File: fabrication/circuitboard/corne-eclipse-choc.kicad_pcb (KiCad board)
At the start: 2 copper layers, 275.5 x 105.6 mm, 182 parts, among them J2 OLED, J4 OLED, SW1 SW_Choc_v1v2_HS, SW10 SW_Choc_v1v2_HS, SW11 SW_Choc_v1v2_HS, SW12 SW_Choc_v1v2_HS, SW13 SW_Choc_v1v2_HS, SW14 SW_Choc_v1v2_HS, SW15 SW_Choc_v1v2_HS, SW16 SW_Choc_v1v2_HS, SW17 SW_Choc_v1v2_HS, SW18 SW_Choc_v1v2_HS, SW2 SW_Choc_v1v2_HS, SW20 SW_Choc_v1v2_HS, SW21 SW_Choc_v1v2_HS, SW22 SW_Choc_v1v2_HS, SW23 SW_Choc_v1v2_HS, SW24 SW_Choc_v1v2_HS, SW25 SW_Choc_v1v2_HS, SW26 SW_Choc_v1v2_HS, SW27 SW_Choc_v1v2_HS, SW28 SW_Choc_v1v2_HS, SW29 SW_Choc_v1v2_HS, SW3 SW_Choc_v1v2_HS, SW30 SW_Choc_v1v2_HS, SW31 SW_Choc_v1v2_HS, SW32 SW_Choc_v1v2_HS, SW33 SW_Choc_v1v2_HS, SW34 SW_Choc_v1v2_HS, SW35 SW_Choc_v1v2_HS, SW36 SW_Choc_v1v2_HS, SW37 SW_Choc_v1v2_HS, SW38 SW_Choc_v1v2_HS, SW39 SW_Choc_v1v2_HS, SW4 SW_Choc_v1v2_HS, SW40 SW_Choc_v1v2_HS, SW42 SW_Choc_v1v2_HS, SW43 SW_Choc_v1v2_HS, SW44 SW_Choc_v1v2_HS, SW5 SW_Choc_v1v2_HS, SW6 SW_Choc_v1v2_HS, SW7 SW_Choc_v1v2_HS, SW8 SW_Choc_v1v2_HS, SW9 SW_Choc_v1v2_HS, U1 nice!nano, U2 nice!nano

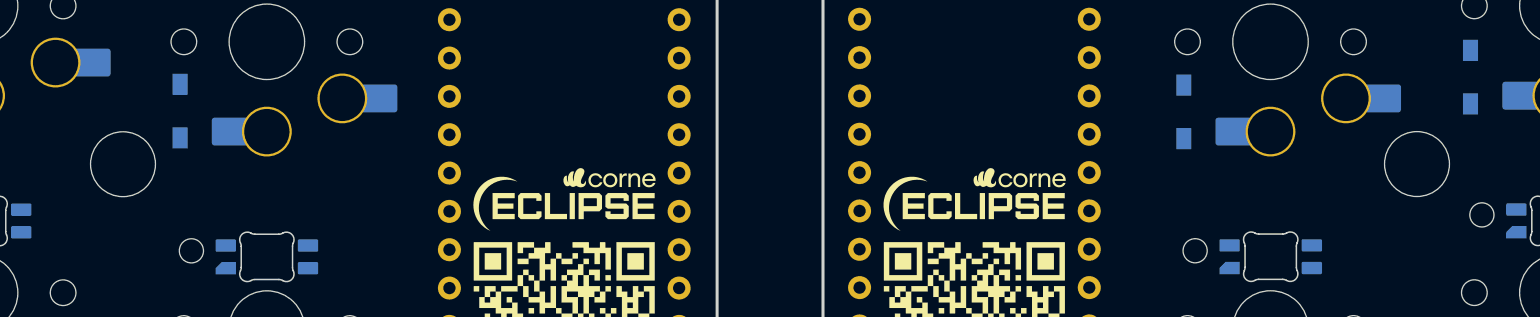
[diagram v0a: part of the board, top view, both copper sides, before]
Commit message: fix(pcb): screw hole alignment to case adjustments
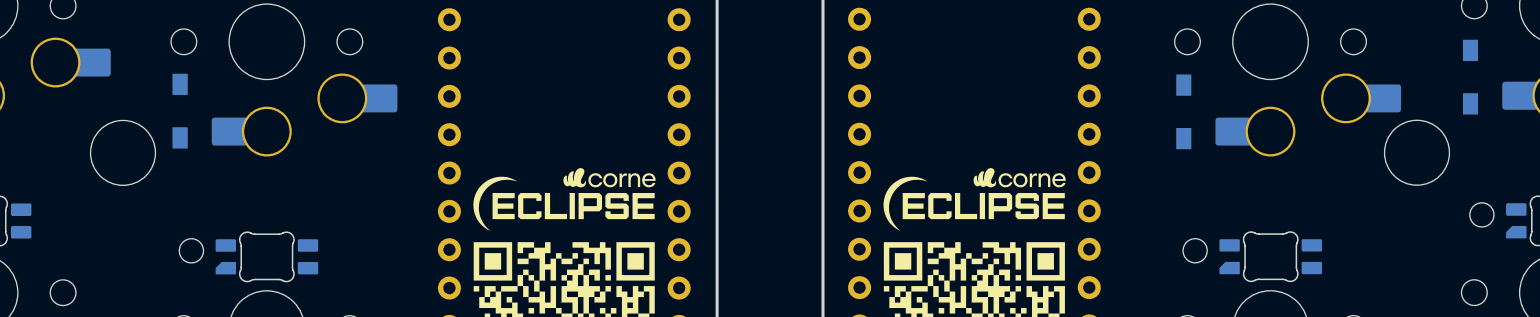
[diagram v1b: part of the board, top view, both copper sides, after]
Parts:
- moved MH1 0.75 mm to (105.6, 40.0)
- moved MH9 0.75 mm to (191.3, 40.0)

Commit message: wip: rgb/choc
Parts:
- moved GLOW06 23.2 mm to (118.5, 97.2)
- moved GLOW02 22.7 mm to (29.8, 32.1)
- moved GLOW01 19.3 mm to (51.0, 38.2)
- moved GLOW03 14.8 mm to (20.2, 63.4), turned to 0 degrees
- moved GLOW05 5.63 mm to (67.2, 77.7), turned to 0 degrees
- moved GLOW04 1.01 mm to (46.3, 64.4), turned to 0 degrees

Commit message: fix(pcbs): aligned screw holes on lp and mx
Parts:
- added BT1: Breakaway_Tabs, kbd:Breakaway_Tabs, F.Cu at (187.0, 20.9)
- added BT2: Breakaway_Tabs, kbd:Breakaway_Tabs, F.Cu at (225.0, 20.9)
- added BT3: Breakaway_Tabs, kbd:Breakaway_Tabs, F.Cu at (148.9, 82.2)
- added BT4: Breakaway_Tabs, kbd:Breakaway_Tabs, F.Cu at (170.9, 82.2)
- added ENC1: ENC_SW_EC12_Choc, Corne Eclipse:ENC_SW_EC12_Choc_v1v2_HS_1u, F.Cu at (196.0, 87.6)
- added J2: OLED, corne:nice!view, F.Cu at (258.3, 62.7)
- added MH1: Val**, kbd:M2_HOLE_v2, F.Cu at (234.3, 40.2)
- added MH10: Val**, kbd:M2_HOLE_v2, F.Cu at (156.3, 53.4)
- added MH11: Val**, kbd:M2_HOLE_v2, F.Cu at (158.4, 44.5)
- added MH12: Val**, kbd:M2_HOLE_v2, B.Cu at (283.3, 82.2)
- added MH2: Val**, kbd:M2_HOLE_v2, F.Cu at (201.5, 80.6)
- added MH3: Val**, kbd:M2_HOLE_v2, F.Cu at (248.1, 88.4)
- added MH4: Val**, kbd:M2_HOLE_v2, F.Cu at (256.6, 73.3)
- added MH5: Val**, kbd:M2_HOLE_v2, F.Cu at (271.0, 81.8)
- added PWR1: , corne:power, F.Cu at (271.8, 74.9)
- added RSW1: SW_PUSH, kbd:ResetSW_1side, F.Cu at (271.5, 65.2)
- added RSW2: SW_PUSH, kbd:ResetSW_1side, F.Cu at (282.9, 65.6)
- added SW1: SW_Choc_v1v2_HS, Corne Eclipse:SW_Choc_v1v2_HS_1u, F.Cu at (148.9, 34.8)
- added SW10: SW_Choc_v1v2_HS, Corne Eclipse:SW_Choc_v1v2_HS_1u, F.Cu at (205.9, 46.7)
- added SW11: SW_Choc_v1v2_HS, Corne Eclipse:SW_Choc_v1v2_HS_1u, F.Cu at (224.9, 49.1)
- added SW12: SW_Choc_v1v2_HS, Corne Eclipse:SW_Choc_v1v2_HS_1u, F.Cu at (243.9, 51.5)
- added SW13: SW_Choc_v1v2_HS, Corne Eclipse:SW_Choc_v1v2_HS_1u, F.Cu at (148.9, 72.8)
- added SW14: SW_Choc_v1v2_HS, Corne Eclipse:SW_Choc_v1v2_HS_1u, F.Cu at (167.9, 72.8)
- added SW15: SW_Choc_v1v2_HS, Corne Eclipse:SW_Choc_v1v2_HS_1u, F.Cu at (186.9, 68.1)
- added SW16: SW_Choc_v1v2_HS, Corne Eclipse:SW_Choc_v1v2_HS_1u, F.Cu at (203.2, 75.1)
- added SW17: SW_Choc_v1v2_HS, Corne Eclipse:SW_Choc_v1v2_HS_1u, F.Cu at (224.9, 68.1)
- added SW18: SW_Choc_v1v2_HS, Corne Eclipse:SW_Choc_v1v2_HS_1u, F.Cu at (243.9, 70.5)
- added SW2: SW_Choc_v1v2_HS, Corne Eclipse:SW_Choc_v1v2_HS_1u, F.Cu at (167.9, 34.8)
- added SW20: SW_Choc_v1v2_HS, Corne Eclipse:SW_Choc_v1v2_HS_1u, F.Cu at (215.4, 87.7)
- added SW21: SW_Choc_v1v2_HS, Corne Eclipse:SW_Choc_v1v2_HS_1u, F.Cu at (236.4, 90.5)
- added SW22: SW_Choc_v1v2_HS, Corne Eclipse:SW_Choc_v1v2_HS_1.5u, F.Cu at (258.6, 94.2)
- added SW3: SW_Choc_v1v2_HS, Corne Eclipse:SW_Choc_v1v2_HS_1u, F.Cu at (186.9, 30.1)
- added SW4: SW_Choc_v1v2_HS, Corne Eclipse:SW_Choc_v1v2_HS_1u, F.Cu at (205.9, 27.7)
- added SW5: SW_Choc_v1v2_HS, Corne Eclipse:SW_Choc_v1v2_HS_1u, F.Cu at (224.9, 30.1)
- added SW6: SW_Choc_v1v2_HS, Corne Eclipse:SW_Choc_v1v2_HS_1u, F.Cu at (243.9, 32.5)
- added SW7: SW_Choc_v1v2_HS, Corne Eclipse:SW_Choc_v1v2_HS_1u, F.Cu at (148.9, 53.8)
- added SW8: SW_Choc_v1v2_HS, Corne Eclipse:SW_Choc_v1v2_HS_1u, F.Cu at (167.9, 53.8)
- added SW9: SW_Choc_v1v2_HS, Corne Eclipse:SW_Choc_v1v2_HS_1u, F.Cu at (186.9, 49.1)
- added TP2: Tenting Puck, Corne Eclipse:Tenting_Puck, F.Cu at (216.2, 57.6)
- added U1: nice!nano, kbd:ProMicro_v3, F.Cu at (263.6, 45.5)
- moved GLOW06 23.2 mm to (103.7, 79.3)
- moved GLOW02 22.7 mm to (51.3, 39.5)
- moved GLOW01 19.3 mm to (70.2, 36.5)
- moved GLOW03 14.8 mm to (29.2, 51.7), turned to 90 degrees
- moved SW16 9.81 mm to (74.4, 75.1)
- moved GLOW05 5.63 mm to (72.8, 78.2), turned to 90 degrees
- moved GLOW04 1.01 mm to (46.8, 63.5), turned to 90 degrees
- moved MH13 0.57 mm to (269.4, 53.7)
- moved MH8 0.57 mm to (267.3, 44.9)
- moved MH9 0.52 mm to (191.3, 40.5)
- moved BT5 0.37 mm to (276.7, 82.6)
- moved MH12 0.37 mm to (154.6, 82.2)
- moved MH14 0.37 mm to (169.0, 73.6)
- moved MH6 0.37 mm to (177.6, 88.8)
- moved SW35 0.37 mm to (276.6, 73.2)
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
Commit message: wip(pcbs): choc layout done, mx layout started
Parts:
- removed the BT1 at (187.0, 20.9)
- removed the BT2 at (225.0, 20.9)
- removed the BT3 at (148.9, 82.2)
- removed the BT4 at (170.9, 82.2)
- removed the ENC1 at (196.0, 87.6)
- removed the J2 at (258.3, 62.7)
- removed the MH1 at (234.3, 40.2)
- removed the MH10 at (156.3, 53.4)
- removed the MH11 at (158.4, 44.5)
- removed the MH12 at (283.3, 82.2)
- removed the MH2 at (201.5, 80.6)
- removed the MH3 at (248.1, 88.4)
- removed the MH4 at (256.6, 73.3)
- removed the MH5 at (271.0, 81.8)
- removed the PWR1 at (271.8, 74.9)
- removed the RSW1 at (271.5, 65.2)
- removed the RSW2 at (282.9, 65.6)
- removed the SW1 at (148.9, 34.8)
- removed the SW10 at (205.9, 46.7)
- removed the SW11 at (224.9, 49.1)
- removed the SW12 at (243.9, 51.5)
- removed the SW13 at (148.9, 72.8)
- removed the SW14 at (167.9, 72.8)
- removed the SW15 at (186.9, 68.1)
- removed the SW16 at (203.2, 75.1)
- removed the SW17 at (224.9, 68.1)
- removed the SW18 at (243.9, 70.5)
- removed the SW2 at (167.9, 34.8)
- removed the SW20 at (215.4, 87.7)
- removed the SW21 at (236.4, 90.5)
- removed the SW22 at (258.6, 94.2)
- removed the SW3 at (186.9, 30.1)
- removed the SW4 at (205.9, 27.7)
- removed the SW5 at (224.9, 30.1)
- removed the SW6 at (243.9, 32.5)
- removed the SW7 at (148.9, 53.8)
- removed the SW8 at (167.9, 53.8)
- removed the SW9 at (186.9, 49.1)
- removed the TP2 at (216.2, 57.6)
- removed the U1 at (263.6, 45.5)
- moved GLOW01 22.4 mm to (118.0, 96.6)
- moved GLOW01 22.4 mm to (178.7, 96.6), turned to -90 degrees
- moved GLOW06 20.0 mm to (86.8, 25.3)
- moved GLOW06 19.9 mm to (210.0, 25.3), turned to -90 degrees
- moved GLOW04 19.5 mm to (29.5, 32.2)
- moved GLOW04 19.5 mm to (267.2, 32.2), turned to -90 degrees
- moved SW16 9.46 mm to (77.1, 66.0)
- moved GLOW02 7.70 mm to (231.7, 77.9), turned to 0 degrees
- moved GLOW02 7.69 mm to (65.1, 77.9), turned to 0 degrees
- moved D19B 7.24 mm to (56.9, 87.5)
- moved D4 4.24 mm to (71.6, 32.0)
- moved D3 1.50 mm to (50.4, 31.8)
- moved GLOW03 0.67 mm to (47.4, 63.6), turned to 0 degrees
- moved GLOW03 0.66 mm to (249.3, 63.6), turned to 0 degrees
- moved D5 0.51 mm to (90.6, 34.3)
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- renumbered GLOW06 to GLOW01, GLOW05 to GLOW02, GLOW04 to GLOW03, GLOW03 to GLOW04, GLOW02 to GLOW05, GLOW01 to GLOW06, SHINE04 to SHINE01, SHINE05 to SHINE02, SHINE12 to SHINE03, SHINE13 to SHINE04, SHINE18 to SHINE05, SHINE19 to SHINE06, SHINE20 to SHINE07, SHINE17 to SHINE08, SHINE14 to SHINE09, SHINE11 to SHINE10, SHINE06 to SHINE11, SHINE03 to SHINE12, SHINE02 to SHINE13, SHINE07 to SHINE14, SHINE10 to SHINE15, SHINE15 to SHINE16, SHINE16 to SHINE17, SHINE21 to SHINE18, SHINE09 to SHINE19, SHINE08 to SHINE20, SHINE01 to SHINE21
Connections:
- GLOW01 pad next: led6-led7 -> led23-led24
- GLOW01 pad prev: led5-led6 -> led21-led23
- GLOW01 pad next: led34-led35 -> led51-led52
- GLOW01 pad prev: led33-led34 -> led49-led51
- GLOW02 pad next: led5-led6 -> led24-led25
- GLOW02 pad prev: led4-led5 -> led23-led24
- GLOW02 pad next: led33-led34 -> led52-led53
- GLOW02 pad prev: led32-led33 -> led51-led52
- GLOW03 pad next: led32-led33 -> led53-led54
- GLOW03 pad prev: led31-led32 -> led52-led53
- GLOW03 pad next: led4-led5 -> led25-led26
- GLOW03 pad prev: led3-led4 -> led24-led25
- GLOW04 pad next: led3-led4 -> led26-led27
- GLOW04 pad prev: led2-led3 -> led25-led26
- GLOW04 pad next: led31-led32 -> led54-led55
- GLOW04 pad prev: led30-led31 -> led53-led54
- GLOW05 pad next: led2-led3 -> led27-led28
- GLOW05 pad prev: led1-led2 -> led26-led27
- GLOW05 pad next: led30-led31 -> led55-led56
- GLOW05 pad prev: led29-led30 -> led54-led55
- GLOW06 pad next: led1-led2 -> (no net)
- GLOW06 pad prev: LED -> led27-led28
- GLOW06 pad next: led29-led30 -> (no net)
- GLOW06 pad prev: LED_r -> led55-led56
- SHINE01 pad 1: led9-led10 -> LED
- SHINE01 pad 4: led10-led11 -> led1-led2
- SHINE01 pad 1: led37-led38 -> LED_r
- SHINE01 pad 4: led38-led39 -> led29-led30
- SHINE02 pad 1: led10-led11 -> led1-led2
- SHINE02 pad 4: led11-led12 -> led2-led3
- SHINE02 pad 1: led38-led39 -> led29-led30
- SHINE02 pad 4: led39-led40 -> led30-led31
- SHINE03 pad 1: led17-led18 -> led2-led3
- SHINE03 pad 4: led18-led19 -> led3-led4
- SHINE03 pad 1: led45-led46 -> led30-led31
- SHINE03 pad 4: led46-led47 -> led31-led32
- SHINE04 pad 1: led18-led19 -> led3-led4
- SHINE04 pad 4: led19-led20 -> led4-led5
- SHINE04 pad 1: led46-led47 -> led31-led32
- SHINE04 pad 4: led47-led48 -> led32-led33
- SHINE05 pad 1: led24-led25 -> led4-led5
- SHINE05 pad 4: led25-led26 -> led5-led6
- SHINE05 pad 1: led52-led53 -> led32-led33
- SHINE05 pad 4: led53-led54 -> led33-led34
- SHINE06 pad 1: led25-led26 -> led5-led6
- SHINE06 pad 4: led26-led27 -> led6-led7
- SHINE06 pad 1: led53-led54 -> led33-led34
- SHINE06 pad 4: led54-led55 -> led34-led35
- SHINE07 pad 1: led26-led27 -> led6-led7
- SHINE07 pad 4: led27-led28 -> led7-led8
- SHINE07 pad 1: led54-led55 -> led34-led35
- SHINE07 pad 4: led55-led56 -> led35-led36
- SHINE08 pad 1: led23-led24 -> led7-led8
- SHINE08 pad 4: led24-led25 -> led8-led9
- SHINE08 pad 1: led51-led52 -> led35-led36
- SHINE08 pad 4: led52-led53 -> led36-led37
- SHINE09 pad 1: led19-led20 -> led8-led9
- SHINE09 pad 4: led20-led21 -> led9-led10
- SHINE09 pad 1: led47-led48 -> led36-led37
- SHINE09 pad 4: led48-led49 -> led37-led38
- SHINE10 pad 1: led16-led17 -> led9-led10
- SHINE10 pad 4: led17-led18 -> led10-led11
- SHINE10 pad 1: led44-led45 -> led37-led38
- SHINE10 pad 4: led45-led46 -> led38-led39
- SHINE11 pad 1: led11-led12 -> led10-led11
- SHINE11 pad 4: led12-led13 -> led11-led12
- SHINE11 pad 1: led39-led40 -> led38-led39
- SHINE11 pad 4: led40-led41 -> led39-led40
- SHINE12 pad 1: led8-led9 -> led11-led12
- SHINE12 pad 4: led9-led10 -> led12-led13
- SHINE12 pad 1: led36-led37 -> led39-led40
- SHINE12 pad 4: led37-led38 -> led40-led41
- SHINE13 pad 1: led7-led8 -> led12-led13
- SHINE13 pad 4: led8-led9 -> led13-led14
- SHINE13 pad 1: led35-led36 -> led40-led41
- SHINE13 pad 4: led36-led37 -> led41-led42
- SHINE14 pad 1: led40-led41 -> led41-led42
- SHINE14 pad 4: led41-led42 -> led42-led43
- SHINE14 pad 1: led12-led13 -> led13-led14
- SHINE14 pad 4: led13-led14 -> led14-led15
- SHINE15 pad 1: led15-led16 -> led14-led15
- SHINE15 pad 4: led16-led17 -> led15-led16
- SHINE15 pad 1: led43-led44 -> led42-led43
- SHINE15 pad 4: led44-led45 -> led43-led44
- SHINE16 pad 1: led20-led21 -> led15-led16
- SHINE16 pad 4: led21-led23 -> led16-led17
- SHINE16 pad 1: led48-led49 -> led43-led44
- SHINE16 pad 4: led49-led51 -> led44-led45
- SHINE17 pad 1: led21-led23 -> led16-led17
- SHINE17 pad 4: led23-led24 -> led17-led18
- SHINE17 pad 1: led49-led51 -> led44-led45
- SHINE17 pad 4: led51-led52 -> led45-led46
- SHINE18 pad 1: led27-led28 -> led17-led18
- SHINE18 pad 4: (no net) -> led18-led19
- SHINE18 pad 1: led55-led56 -> led45-led46
- SHINE18 pad 4: (no net) -> led46-led47
- SHINE19 pad 1: led42-led43 -> led46-led47
- SHINE19 pad 4: led43-led44 -> led47-led48
- SHINE19 pad 1: led14-led15 -> led18-led19
- SHINE19 pad 4: led15-led16 -> led19-led20
- SHINE20 pad 1: led41-led42 -> led47-led48
- SHINE20 pad 4: led42-led43 -> led48-led49
- SHINE20 pad 1: led13-led14 -> led19-led20
- SHINE20 pad 4: led14-led15 -> led20-led21
- SHINE21 pad 1: led6-led7 -> led20-led21
- SHINE21 pad 4: led7-led8 -> led21-led23
- SHINE21 pad 1: led34-led35 -> led48-led49
- SHINE21 pad 4: led35-led36 -> led49-led51

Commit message: feat(pcb): wiring ready
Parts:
- moved R2 1.01 mm to (170.1, 69.0)
- moved RGBMOS 1.01 mm to (170.1, 65.8)
- moved R1 1.00 mm to (126.7, 69.0)
- moved RGBMOS 1.00 mm to (126.7, 65.8)
- moved J4 0.56 mm to (156.7, 62.6)
- moved GLOW06 0.50 mm to (210.0, 25.8)
- moved GLOW06 0.50 mm to (86.8, 25.8)
